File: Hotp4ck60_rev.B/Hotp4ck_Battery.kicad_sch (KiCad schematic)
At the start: 20 parts, among them J3 Conn_01x02_MountingPin, Q1 2N7002, SW2 PWR, U2 BQ24075, U3 MAX17048

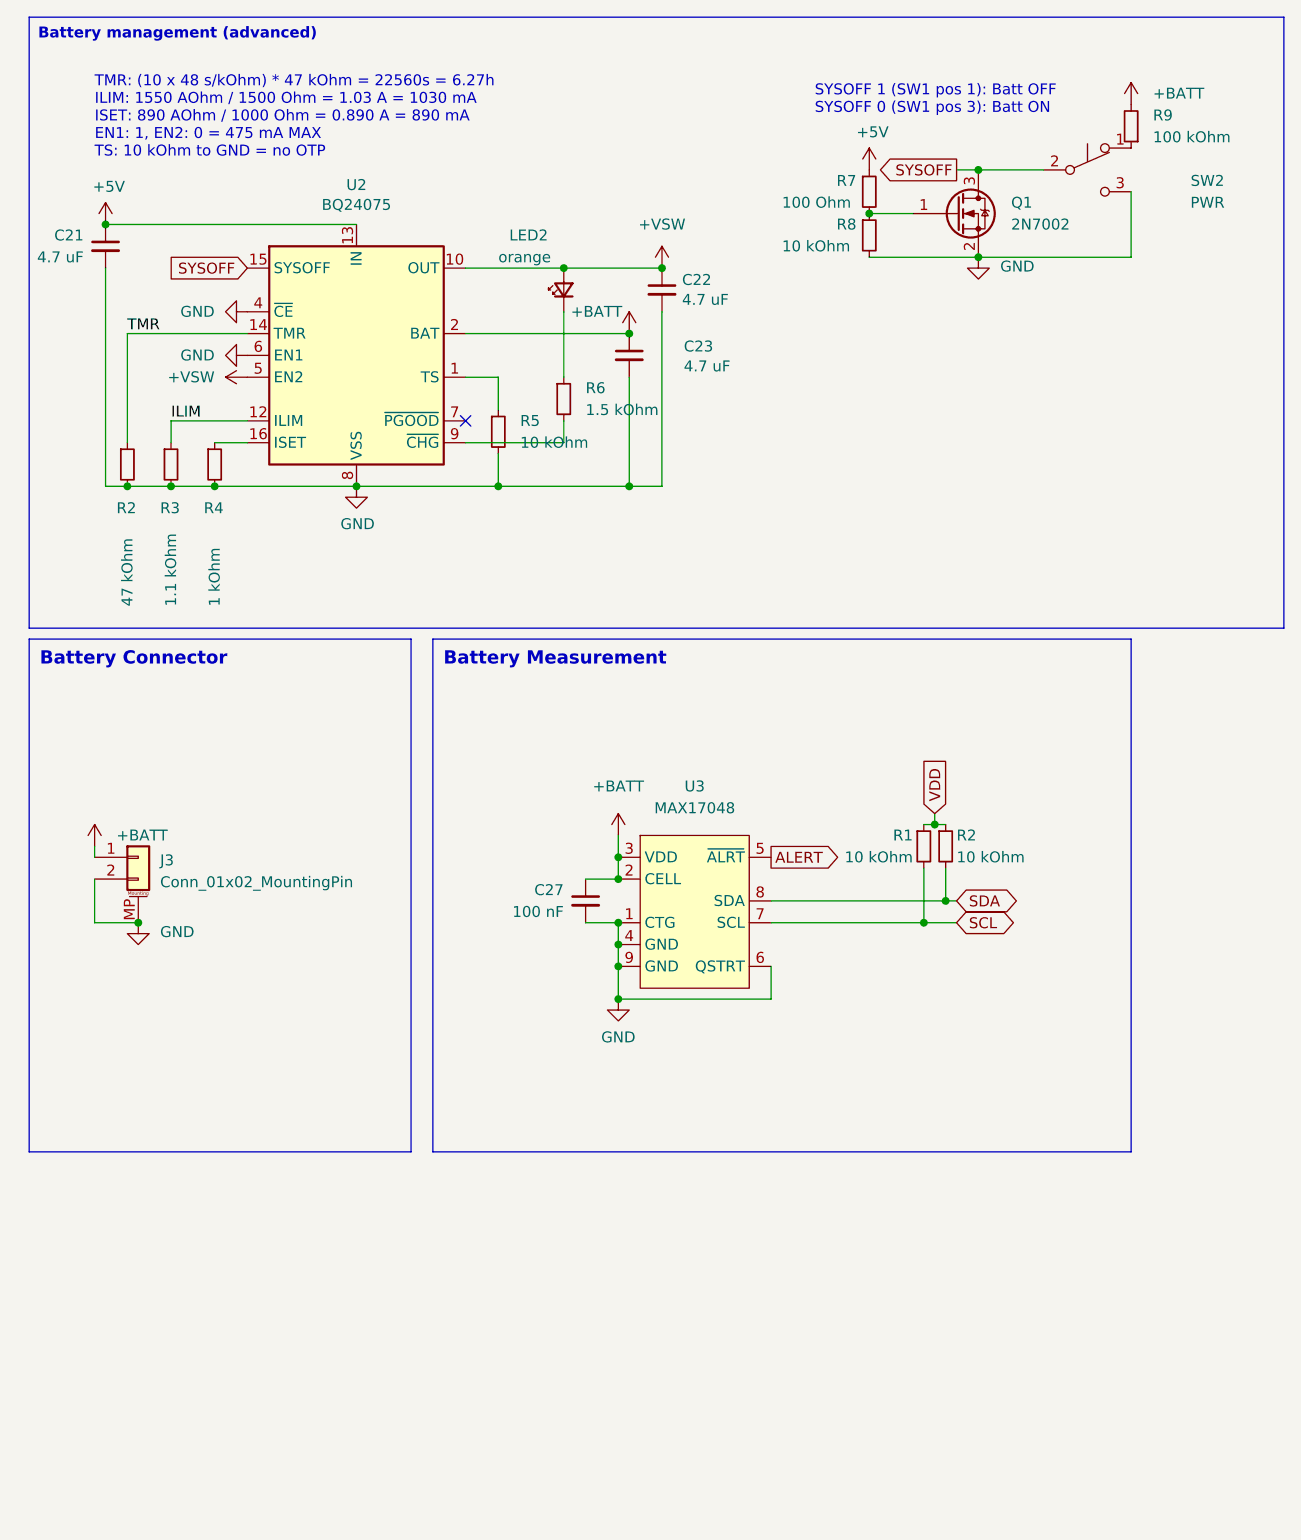
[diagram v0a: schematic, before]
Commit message: Change to daugtherboard
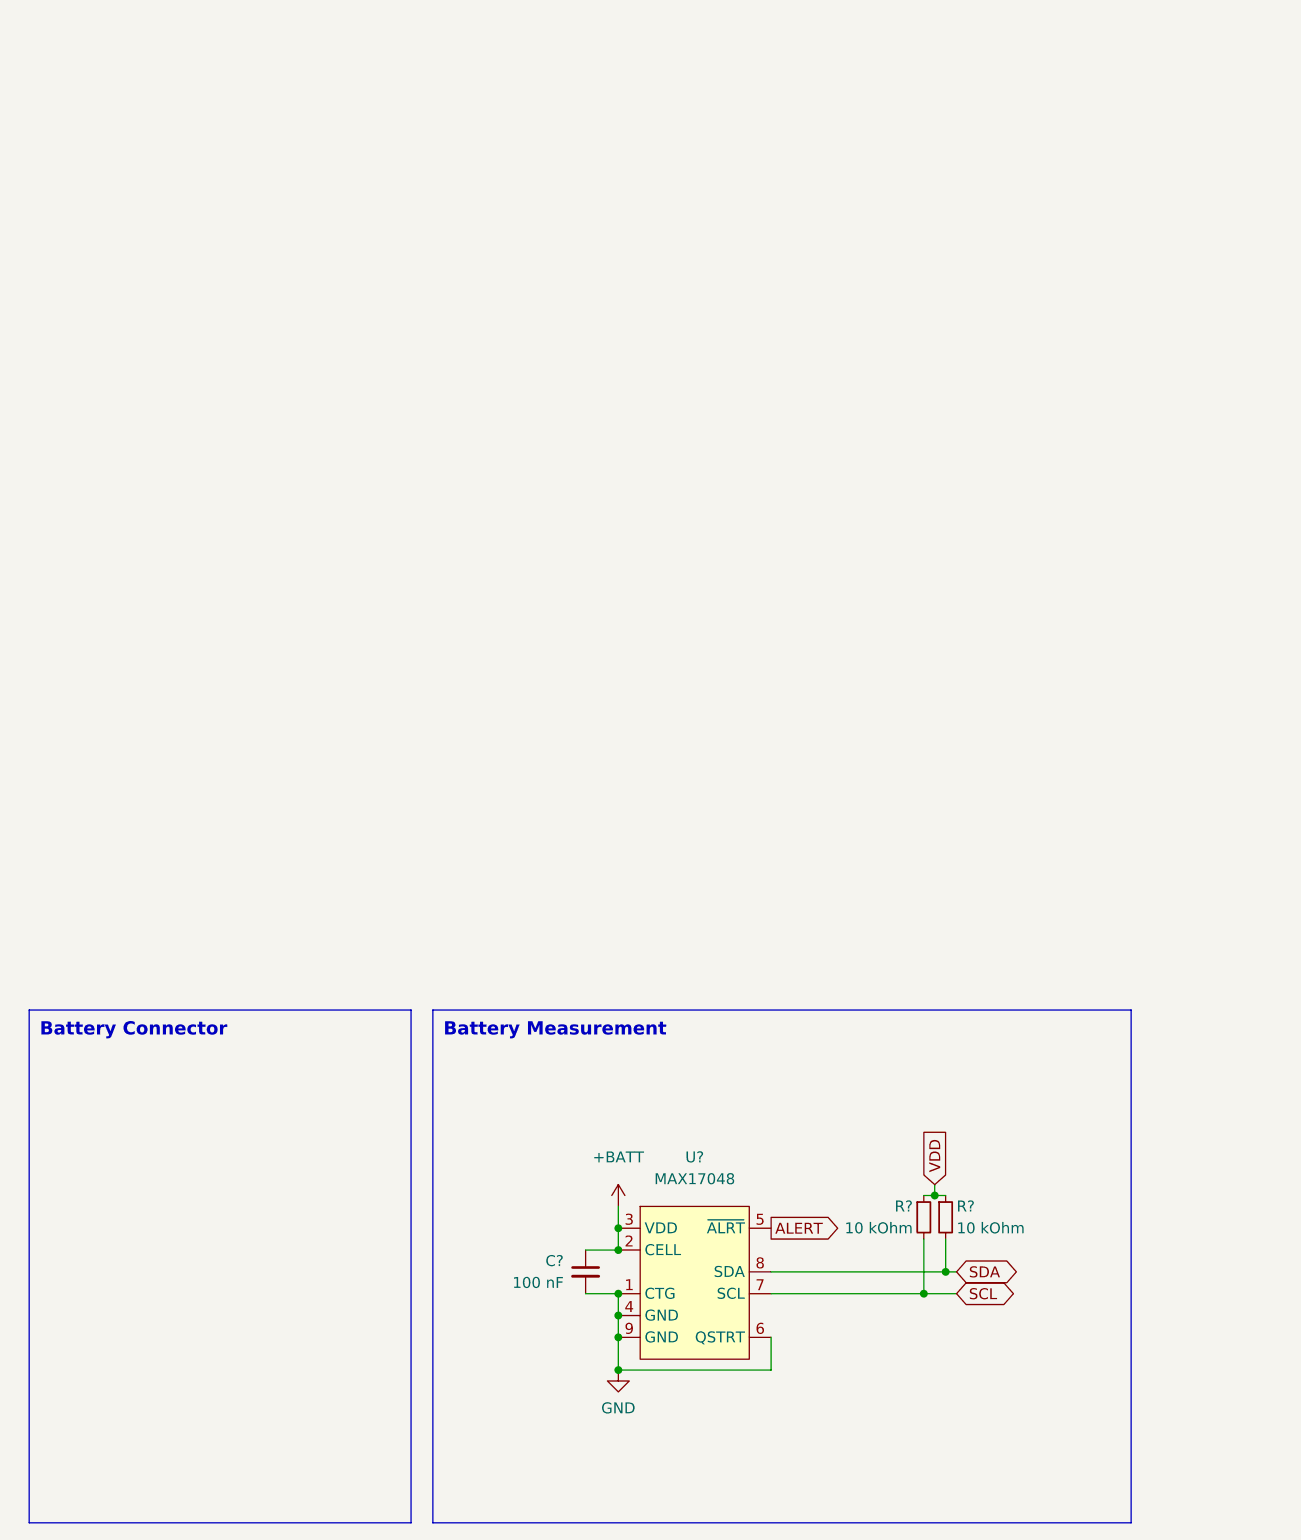
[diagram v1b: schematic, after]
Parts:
- removed C21, C22, C23: 4.7 uF, Capacitor_SMD:C_0402_1005Metric, symbol Device:C_Small
- removed J3: Conn_01x02_MountingPin, Connector_Molex:Molex_PicoBlade_53261-0271_1x02-1MP_P1.25mm_Horizontal, symbol Connector_Generic_MountingPin:Conn_01x02_MountingPin
- removed LED2: orange, LED_SMD:LED_0603_1608Metric, symbol Device:LED_Small
- removed Q1: 2N7002, Package_TO_SOT_SMD:SOT-23, symbol Transistor_FET:2N7002
- removed R2: 47 kOhm, Resistor_SMD:R_0402_1005Metric, symbol Device:R_Small
- removed R3: 1.1 kOhm, Resistor_SMD:R_0402_1005Metric, symbol Device:R_Small
- removed R4: 1 kOhm, Resistor_SMD:R_0402_1005Metric, symbol Device:R_Small
- removed R5, R8: 10 kOhm, Resistor_SMD:R_0402_1005Metric, symbol Device:R_Small
- removed R6: 1.5 kOhm, Resistor_SMD:R_0402_1005Metric, symbol Device:R_Small
- removed R7: 100 Ohm, Resistor_SMD:R_0402_1005Metric, symbol Device:R_Small
- removed R9: 100 kOhm, Resistor_SMD:R_0402_1005Metric, symbol Device:R_Small
- removed SW2: PWR, PCM_marbastlib-various:SW_MSK12C02-HB, symbol Switch:SW_Push_SPDT
- removed U2: BQ24075, Package_DFN_QFN:VQFN-16-1EP_3x3mm_P0.5mm_EP1.6x1.6mm, symbol Battery_Management:BQ24075RGT
- renumbered C27 to C?, R2 to R?, R1 to R?, U3 to U?
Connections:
- no-connect marks 1 -> 0
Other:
- note removed: "SYSOFF 1 (SW1 pos 1): Batt OFF SYSOFF 0 (SW1 pos 3): Batt ON"
- note removed: "TMR: (10 x 48 s/kOhm) * 47 kOhm = 22560s = 6.27h ILIM: 1550 AOhm / 1500 Ohm = 1.03 A = 1030 mA ISET: 890 AOhm / 1000 Ohm = 0.890 A = 890 mA EN1: 1, EN2: 0 = 475 mA MAX TS: 10 kOhm to GND = no OTP"
- moved on the sheet: C?, R?, U?
